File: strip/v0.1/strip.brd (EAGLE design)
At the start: 67 x 11.5 mm, 102 parts, among them IC1 LP2992, IC2 ADP3110A-SO8, IC3 MAX3051, IC4 OPA335, IC5 ADP3110A-SO8, IC6 ADP3110A-SO8, IC7 STM32F050CX, Q1 IRF7828, Q2 IRF7828, Q3 IRF7828, Q4 IRF7828, Q5 IRF7828, Q6 IRF7828

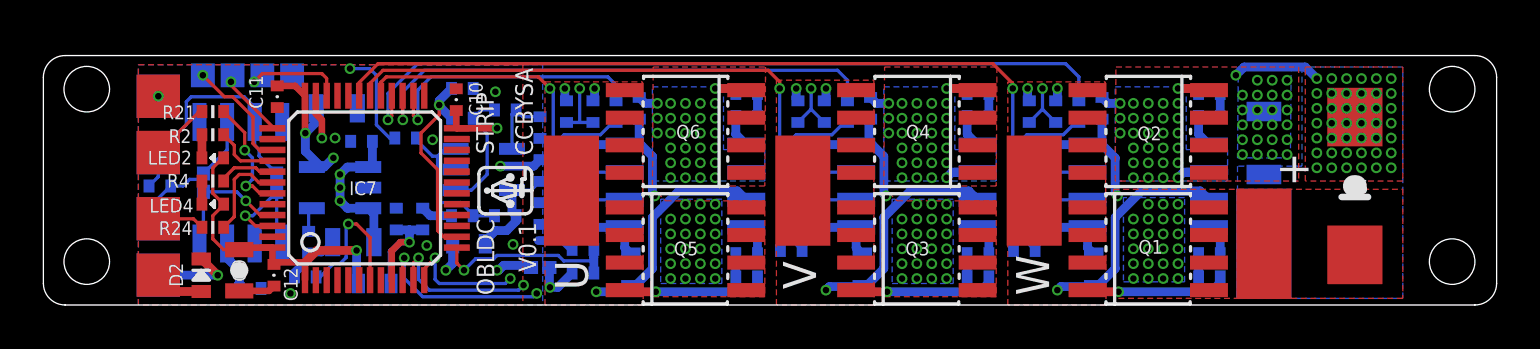
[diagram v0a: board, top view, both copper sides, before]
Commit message: Some minor adjustments and cleanups.
- Vias in hex pattern
- Board .5mm wider for more material between mounting holes and board
  edge.
- Adjusted pours to use more board real estate for more copper in board.
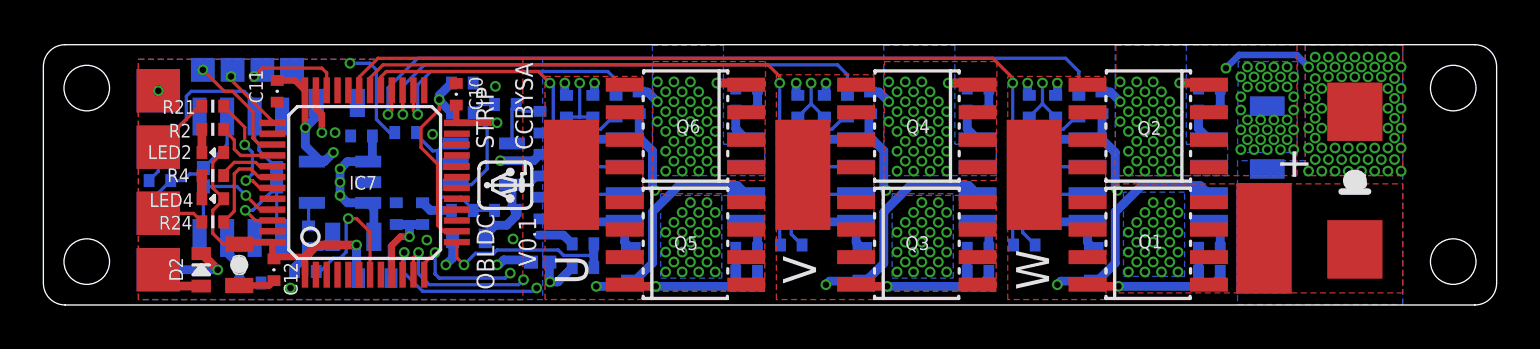
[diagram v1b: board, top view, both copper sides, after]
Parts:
- moved PAD1 0.73 mm to (41.7, 6.00)
- moved PAD2 0.73 mm to (31.0, 6.00)
- moved PAD5 0.73 mm to (20.3, 6.00)
- moved R45 0.29 mm to (52.4, 7.72)
- moved C1 0.25 mm to (10.3, 3.15)
- moved C10 0.25 mm to (15.0, 9.72)
- moved C11 0.25 mm to (6.78, 9.85)
- moved C12 0.25 mm to (6.63, 1.62)
- moved C13 0.25 mm to (5.54, 1.01)
- moved C19 0.25 mm to (18.9, 6.45)
- moved C2 0.25 mm to (10.7, 7.79)
- moved C20 0.25 mm to (15.3, 10.2)
- moved C23 0.25 mm to (23.1, 1.85)
- moved C24 0.25 mm to (33.8, 1.85)
- moved C25 0.25 mm to (44.4, 1.85)
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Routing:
- net PGND: track 55.0 -> 49.3 mm, vias 105 -> 144
- net GND: track 56.2 -> 55.9 mm, vias 55 -> 76
- net BUSS+: vias 73 -> 82
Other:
- board size 67 x 11.5 mm -> 67 x 12 mm

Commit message: Some more layout polishing.
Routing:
- net TMS/SWDIO: track 4.90 -> 4.20 mm
